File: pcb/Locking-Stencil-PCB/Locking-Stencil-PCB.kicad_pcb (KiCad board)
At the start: 2 copper layers, 64 parts

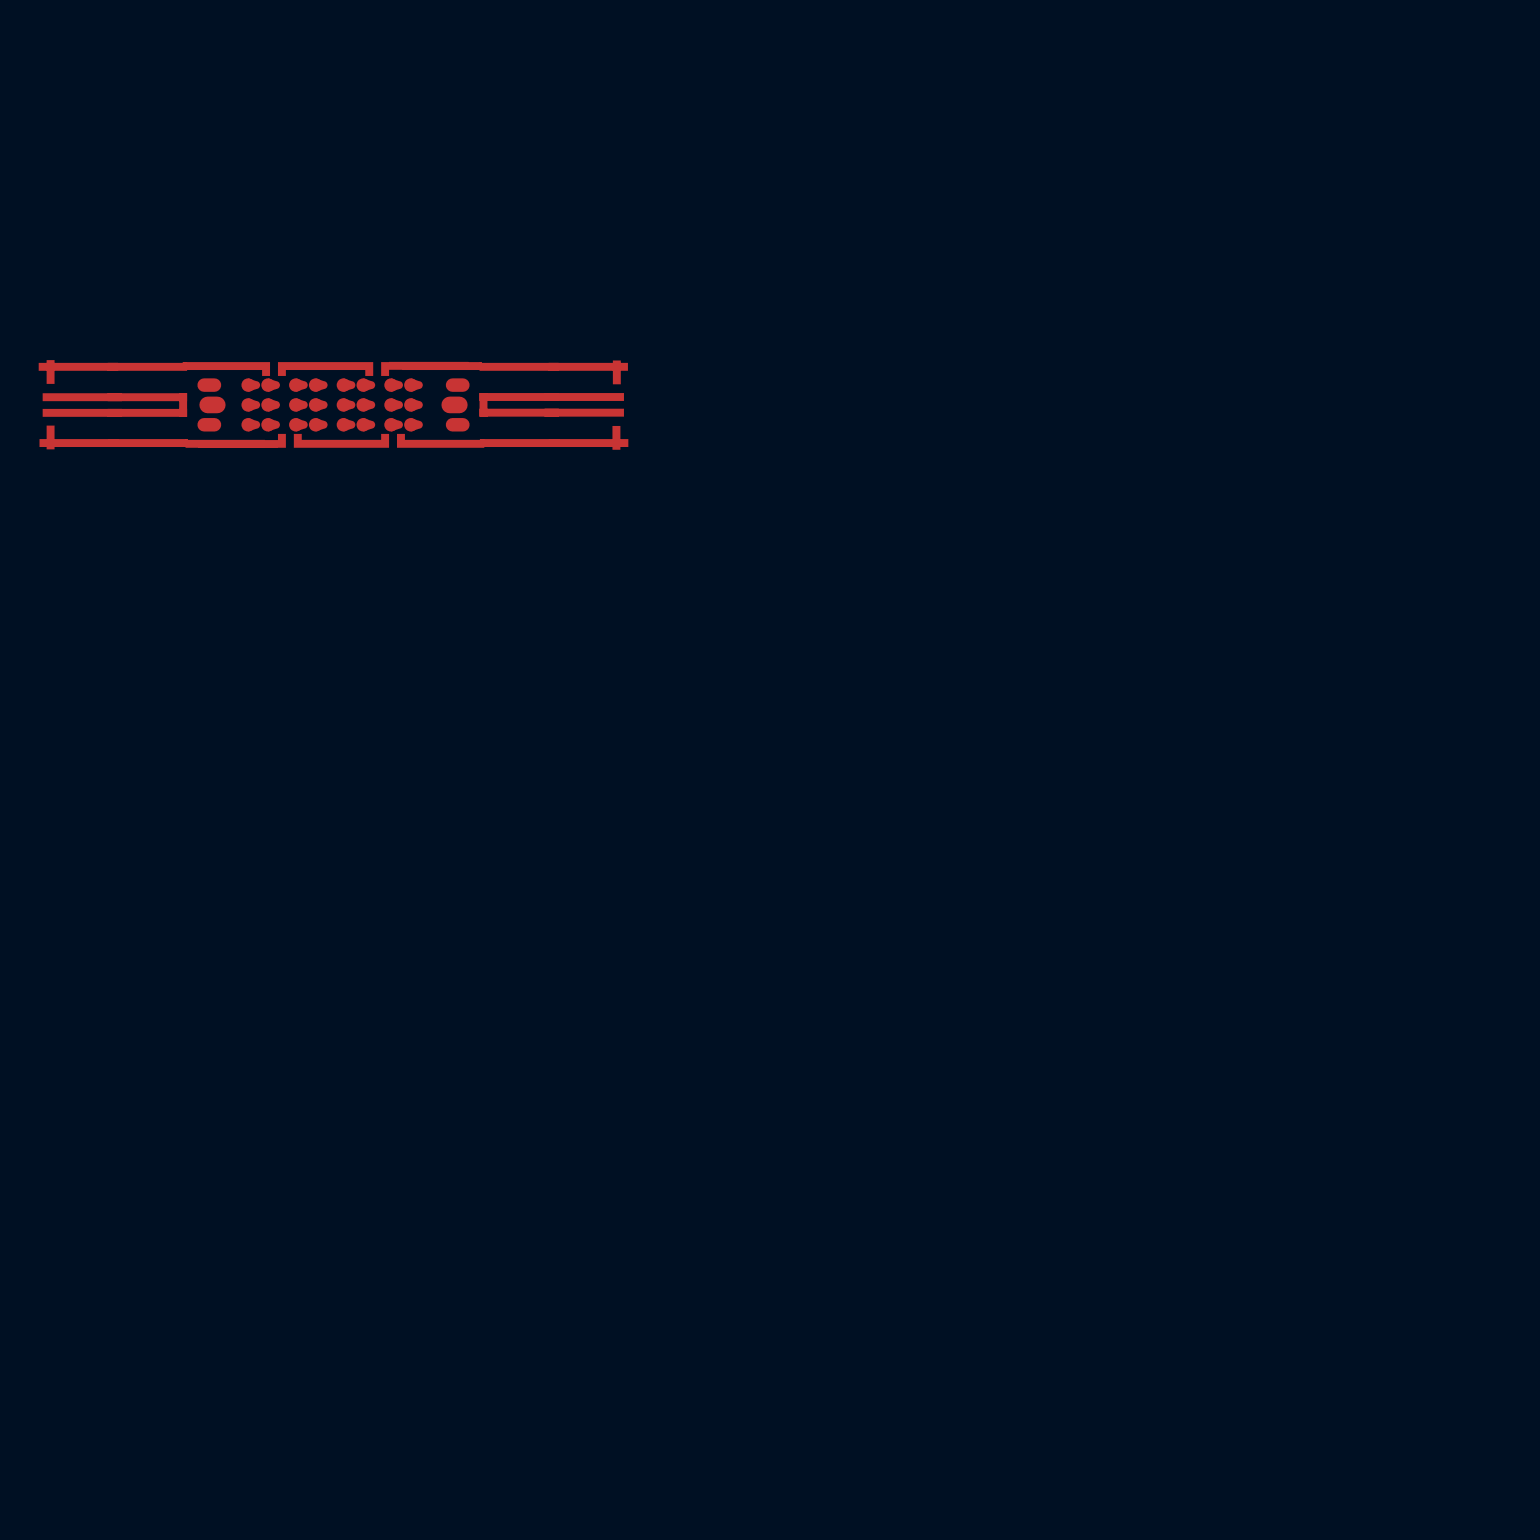
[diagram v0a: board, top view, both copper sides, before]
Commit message: Create stencil order
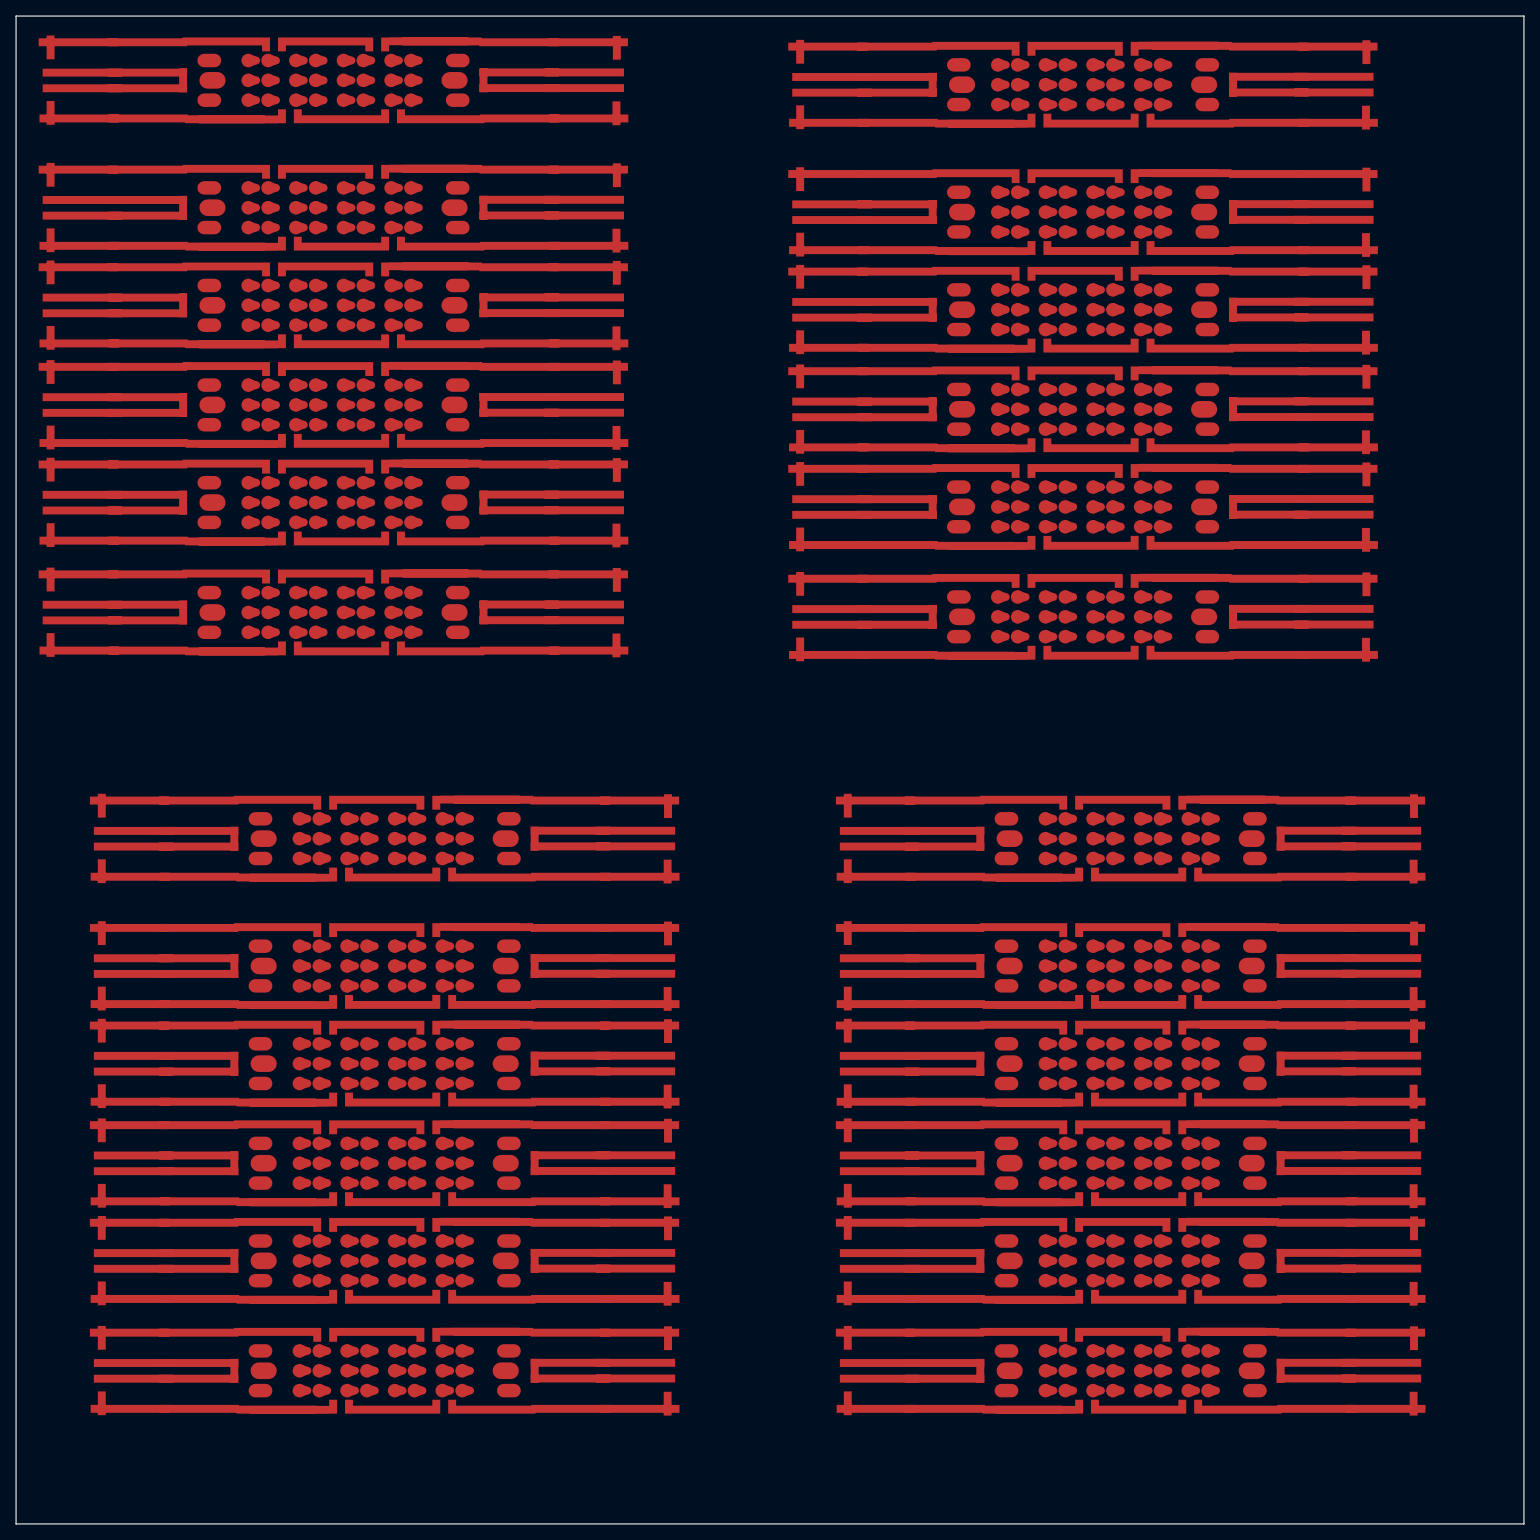
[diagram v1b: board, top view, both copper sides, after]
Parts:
- added REF**: Pad_Cutable_Segment_1mm, 00-stencil-footprint-lib:Pad_Cutable_Segment_1mm, F.Cu at (114.0, 159.1)
- added REF**: Pad_10x1mm, 00-stencil-footprint-lib:Pad_10x1mm, F.Cu at (138.1, 207.3)
- added REF**: Pad_Tapered_d1_1.7mm_d2_1mm_dist_1mm, 00-stencil-footprint-lib:Pad_Tapered_d1_1.7mm_d2_1mm_dist_1mm, F.Cu at (208.2, 195.6)
- added REF**: Pad_10x1mm, 00-stencil-footprint-lib:Pad_10x1mm, F.Cu at (171.0, 71.4)
- added REF**: Pad_Slot_d_1.7mm_dist_1mm, 00-stencil-footprint-lib:Pad_Slot_d_1.7mm_dist_1mm, F.Cu at (216.6, 173.2)
- added REF**: Pad_Slot_d_1.7mm_dist_1mm, 00-stencil-footprint-lib:Pad_Slot_d_1.7mm_dist_1mm, F.Cu at (185.3, 198.1)
- added REF**: Pad_10x1mm, 00-stencil-footprint-lib:Pad_10x1mm, F.Cu at (195.4, 131.1)
- added REF**: Pad_10x1mm, 00-stencil-footprint-lib:Pad_10x1mm, F.Cu at (74.8, 208.3)
- added REF**: Pad_10x1mm, 00-stencil-footprint-lib:Pad_10x1mm, F.Cu at (168.8, 171.2)
- added REF**: Pad_Slot_d_2.1mm_dist_1mm, 00-stencil-footprint-lib:Pad_Slot_d_2.1mm_dist_1mm, F.Cu at (122.2, 170.7)
- added REF**: Pad_10x1mm, 00-stencil-footprint-lib:Pad_10x1mm, F.Cu at (180.8, 131.1)
- added REF**: Pad_Tapered_d1_1.7mm_d2_1mm_dist_1mm, 00-stencil-footprint-lib:Pad_Tapered_d1_1.7mm_d2_1mm_dist_1mm, F.Cu at (110.2, 77.7)
- added REF**: Pad_Slot_d_1.7mm_dist_1mm, 00-stencil-footprint-lib:Pad_Slot_d_1.7mm_dist_1mm, F.Cu at (216.6, 157.2)
- added REF**: Pad_10x1mm, 00-stencil-footprint-lib:Pad_10x1mm, F.Cu at (83.1, 158.9)
- added REF**: Pad_10x1mm, 00-stencil-footprint-lib:Pad_10x1mm, F.Cu at (168.4, 212.2)
- added REF**: Pad_10x1mm, 00-stencil-footprint-lib:Pad_10x1mm, F.Cu at (217.8, 89.5)
- added REF**: Pad_Slot_d_1.7mm_dist_1mm, 00-stencil-footprint-lib:Pad_Slot_d_1.7mm_dist_1mm, F.Cu at (210.6, 62.1)
- added REF**: Pad_3x1mm, 00-stencil-footprint-lib:Pad_3x1mm, F.Cu at (219.8, 170.7)
- added REF**: Pad_10x1mm, 00-stencil-footprint-lib:Pad_10x1mm, F.Cu at (168.8, 194.1)
- added REF**: Pad_Tapered_d1_1.7mm_d2_1mm_dist_1mm, 00-stencil-footprint-lib:Pad_Tapered_d1_1.7mm_d2_1mm_dist_1mm, F.Cu at (196.2, 168.2)
- added REF**: Pad_3x1mm, 00-stencil-footprint-lib:Pad_3x1mm, F.Cu at (175.0, 88.0)
- added REF**: Pad_10x1mm, 00-stencil-footprint-lib:Pad_10x1mm, F.Cu at (107.5, 175.1)
- added REF**: Pad_3x1mm, 00-stencil-footprint-lib:Pad_3x1mm, F.Cu at (219.8, 154.7)
- added REF**: Pad_10x1mm, 00-stencil-footprint-lib:Pad_10x1mm, F.Cu at (171.0, 58.2)
- added REF**: Pad_10x1mm, 00-stencil-footprint-lib:Pad_10x1mm, F.Cu at (92.5, 166.3)
- added REF**: Pad_10x1mm, 00-stencil-footprint-lib:Pad_10x1mm, F.Cu at (162.8, 111.4)
- added REF**: Pad_10x1mm, 00-stencil-footprint-lib:Pad_10x1mm, F.Cu at (131.6, 125.7)
- added REF**: Pad_10x1mm, 00-stencil-footprint-lib:Pad_10x1mm, F.Cu at (214.4, 199.9)
- added REF**: Pad_10x1mm, 00-stencil-footprint-lib:Pad_10x1mm, F.Cu at (223.8, 221.2)
- added REF**: Pad_Tapered_d1_1.7mm_d2_1mm_dist_1mm, 00-stencil-footprint-lib:Pad_Tapered_d1_1.7mm_d2_1mm_dist_1mm, F.Cu at (92.2, 90.0)
- added REF**: Pad_Slot_d_1.7mm_dist_1mm, 00-stencil-footprint-lib:Pad_Slot_d_1.7mm_dist_1mm, F.Cu at (116.2, 114.8)
- added REF**: Pad_Slot_d_1.7mm_dist_1mm, 00-stencil-footprint-lib:Pad_Slot_d_1.7mm_dist_1mm, F.Cu at (116.2, 85.0)
- added REF**: Pad_Tapered_d1_1.7mm_d2_1mm_dist_1mm, 00-stencil-footprint-lib:Pad_Tapered_d1_1.7mm_d2_1mm_dist_1mm, F.Cu at (110.2, 109.8)
- added REF**: Pad_Tapered_d1_1.7mm_d2_1mm_dist_1mm, 00-stencil-footprint-lib:Pad_Tapered_d1_1.7mm_d2_1mm_dist_1mm, F.Cu at (196.2, 62.1)
- added REF**: Pad_Tapered_d1_1.7mm_d2_1mm_dist_1mm, 00-stencil-footprint-lib:Pad_Tapered_d1_1.7mm_d2_1mm_dist_1mm, F.Cu at (204.7, 73.2)
- added REF**: Pad_Tapered_d1_1.7mm_d2_1mm_dist_1mm, 00-stencil-footprint-lib:Pad_Tapered_d1_1.7mm_d2_1mm_dist_1mm, F.Cu at (210.7, 185.5)
- added REF**: Pad_Cutable_Segment_1mm, 00-stencil-footprint-lib:Pad_Cutable_Segment_1mm, F.Cu at (199.9, 96.2)
- added REF**: Pad_10x1mm, 00-stencil-footprint-lib:Pad_10x1mm, F.Cu at (171.0, 86.5)
- added REF**: Pad_10x1mm, 00-stencil-footprint-lib:Pad_10x1mm, F.Cu at (129.9, 175.0)
- added REF**: Pad_10x1mm, 00-stencil-footprint-lib:Pad_10x1mm, F.Cu at (105.5, 150.2)
- added REF**: Pad_10x1mm, 00-stencil-footprint-lib:Pad_10x1mm, F.Cu at (101.0, 130.6)
- added REF**: Pad_10x1mm, 00-stencil-footprint-lib:Pad_10x1mm, F.Cu at (168.4, 175.0)
- added REF**: Pad_10x1mm, 00-stencil-footprint-lib:Pad_10x1mm, F.Cu at (83.0, 191.2)
- added REF**: Pad_Tapered_d1_1.7mm_d2_1mm_dist_1mm, 00-stencil-footprint-lib:Pad_Tapered_d1_1.7mm_d2_1mm_dist_1mm, F.Cu at (198.7, 154.7)
- added REF**: Pad_Tapered_d1_1.7mm_d2_1mm_dist_1mm, 00-stencil-footprint-lib:Pad_Tapered_d1_1.7mm_d2_1mm_dist_1mm, F.Cu at (104.7, 173.2)
- added REF**: Pad_Tapered_d1_1.7mm_d2_1mm_dist_1mm, 00-stencil-footprint-lib:Pad_Tapered_d1_1.7mm_d2_1mm_dist_1mm, F.Cu at (198.7, 90.5)
- added REF**: Pad_Tapered_d1_1.7mm_d2_1mm_dist_1mm, 00-stencil-footprint-lib:Pad_Tapered_d1_1.7mm_d2_1mm_dist_1mm, F.Cu at (96.2, 210.3)
- added REF**: Pad_10x1mm, 00-stencil-footprint-lib:Pad_10x1mm, F.Cu at (120.5, 212.2)
- added REF**: Pad_Tapered_d1_1.7mm_d2_1mm_dist_1mm, 00-stencil-footprint-lib:Pad_Tapered_d1_1.7mm_d2_1mm_dist_1mm, F.Cu at (208.2, 193.1)
- added REF**: Pad_Tapered_d1_1.7mm_d2_1mm_dist_1mm, 00-stencil-footprint-lib:Pad_Tapered_d1_1.7mm_d2_1mm_dist_1mm, F.Cu at (202.2, 75.7)
- added REF**: Pad_Tapered_d1_1.7mm_d2_1mm_dist_1mm, 00-stencil-footprint-lib:Pad_Tapered_d1_1.7mm_d2_1mm_dist_1mm, F.Cu at (108.2, 224.2)
- added REF**: Pad_Tapered_d1_1.7mm_d2_1mm_dist_1mm, 00-stencil-footprint-lib:Pad_Tapered_d1_1.7mm_d2_1mm_dist_1mm, F.Cu at (104.2, 56.6)
- added REF**: Pad_Cutable_Segment_1mm, 00-stencil-footprint-lib:Pad_Cutable_Segment_1mm, F.Cu at (107.5, 130.6)
- added REF**: Pad_10x1mm, 00-stencil-footprint-lib:Pad_10x1mm, F.Cu at (171.0, 125.2)
- added REF**: Pad_10x1mm, 00-stencil-footprint-lib:Pad_10x1mm, F.Cu at (74.8, 169.2)
- added REF**: Pad_10x1mm, 00-stencil-footprint-lib:Pad_10x1mm, F.Cu at (214.2, 166.3)
- added REF**: Pad_Tapered_d1_1.7mm_d2_1mm_dist_1mm, 00-stencil-footprint-lib:Pad_Tapered_d1_1.7mm_d2_1mm_dist_1mm, F.Cu at (108.2, 180.5)
- added REF**: Pad_Cutable_Segment_1mm, 00-stencil-footprint-lib:Pad_Cutable_Segment_1mm, F.Cu at (92.5, 83.0)
- added REF**: Pad_10x1mm, 00-stencil-footprint-lib:Pad_10x1mm, F.Cu at (186.8, 175.1)
- added REF**: Pad_Tapered_d1_1.7mm_d2_1mm_dist_1mm, 00-stencil-footprint-lib:Pad_Tapered_d1_1.7mm_d2_1mm_dist_1mm, F.Cu at (192.7, 100.5)
- added REF**: Pad_10x1mm, 00-stencil-footprint-lib:Pad_10x1mm, F.Cu at (188.4, 212.3)
- added REF**: Pad_10x1mm, 00-stencil-footprint-lib:Pad_10x1mm, F.Cu at (132.2, 79.5)
- added REF**: Pad_Tapered_d1_1.7mm_d2_1mm_dist_1mm, 00-stencil-footprint-lib:Pad_Tapered_d1_1.7mm_d2_1mm_dist_1mm, F.Cu at (198.7, 221.7)
- added REF**: Pad_Slot_d_2.1mm_dist_1mm, 00-stencil-footprint-lib:Pad_Slot_d_2.1mm_dist_1mm, F.Cu at (216.2, 170.7)
- added REF**: Pad_Tapered_d1_1.7mm_d2_1mm_dist_1mm, 00-stencil-footprint-lib:Pad_Tapered_d1_1.7mm_d2_1mm_dist_1mm, F.Cu at (104.7, 207.8)
- added REF**: Pad_10x1mm, 00-stencil-footprint-lib:Pad_10x1mm, F.Cu at (138.6, 203.6)
- added REF**: Pad_Tapered_d1_1.7mm_d2_1mm_dist_1mm, 00-stencil-footprint-lib:Pad_Tapered_d1_1.7mm_d2_1mm_dist_1mm, F.Cu at (98.2, 56.6)
- added REF**: Pad_3x1mm, 00-stencil-footprint-lib:Pad_3x1mm, F.Cu at (136.2, 108.2)
- added REF**: Pad_10x1mm, 00-stencil-footprint-lib:Pad_10x1mm, F.Cu at (162.8, 58.2)
- added REF**: Pad_10x1mm, 00-stencil-footprint-lib:Pad_10x1mm, F.Cu at (214.4, 175.1)
- added REF**: Pad_3x1mm, 00-stencil-footprint-lib:Pad_3x1mm, F.Cu at (70.3, 203.7)
- added REF**: Pad_Tapered_d1_1.7mm_d2_1mm_dist_1mm, 00-stencil-footprint-lib:Pad_Tapered_d1_1.7mm_d2_1mm_dist_1mm, F.Cu at (89.8, 123.7)
- added REF**: Pad_Tapered_d1_1.7mm_d2_1mm_dist_1mm, 00-stencil-footprint-lib:Pad_Tapered_d1_1.7mm_d2_1mm_dist_1mm, F.Cu at (104.7, 210.3)
- added REF**: Pad_3x1mm, 00-stencil-footprint-lib:Pad_3x1mm, F.Cu at (136.2, 79.3)
- added REF**: Pad_Slot_d_1.7mm_dist_1mm, 00-stencil-footprint-lib:Pad_Slot_d_1.7mm_dist_1mm, F.Cu at (216.6, 180.5)
- added REF**: Pad_Tapered_d1_1.7mm_d2_1mm_dist_1mm, 00-stencil-footprint-lib:Pad_Tapered_d1_1.7mm_d2_1mm_dist_1mm, F.Cu at (186.7, 57.1)
- added REF**: Pad_Tapered_d1_1.7mm_d2_1mm_dist_1mm, 00-stencil-footprint-lib:Pad_Tapered_d1_1.7mm_d2_1mm_dist_1mm, F.Cu at (110.2, 126.2)
- added REF**: Pad_10x1mm, 00-stencil-footprint-lib:Pad_10x1mm, F.Cu at (68.0, 63.4)
- added REF**: Pad_Tapered_d1_1.7mm_d2_1mm_dist_1mm, 00-stencil-footprint-lib:Pad_Tapered_d1_1.7mm_d2_1mm_dist_1mm, F.Cu at (102.2, 173.2)
- added REF**: Pad_10x1mm, 00-stencil-footprint-lib:Pad_10x1mm, F.Cu at (123.4, 87.0)
- added REF**: Pad_Slot_d_1.7mm_dist_1mm, 00-stencil-footprint-lib:Pad_Slot_d_1.7mm_dist_1mm, F.Cu at (185.3, 180.5)
- added REF**: Pad_Slot_d_1.7mm_dist_1mm, 00-stencil-footprint-lib:Pad_Slot_d_1.7mm_dist_1mm, F.Cu at (179.3, 78.2)
- added REF**: Pad_Slot_d_2.1mm_dist_1mm, 00-stencil-footprint-lib:Pad_Slot_d_2.1mm_dist_1mm, F.Cu at (122.2, 183.0)
- added REF**: Pad_10x1mm, 00-stencil-footprint-lib:Pad_10x1mm, F.Cu at (232.6, 212.2)
- added REF**: Pad_Tapered_d1_1.7mm_d2_1mm_dist_1mm, 00-stencil-footprint-lib:Pad_Tapered_d1_1.7mm_d2_1mm_dist_1mm, F.Cu at (101.8, 56.6)
- added REF**: Pad_Tapered_d1_1.7mm_d2_1mm_dist_1mm, 00-stencil-footprint-lib:Pad_Tapered_d1_1.7mm_d2_1mm_dist_1mm, F.Cu at (108.2, 173.2)
- added REF**: Pad_3x1mm, 00-stencil-footprint-lib:Pad_3x1mm, F.Cu at (158.3, 104.7)
- added REF**: Pad_Cutable_Segment_1mm, 00-stencil-footprint-lib:Pad_Cutable_Segment_1mm, F.Cu at (112.0, 203.4)
- added REF**: Pad_10x1mm, 00-stencil-footprint-lib:Pad_10x1mm, F.Cu at (232.1, 207.3)
- added REF**: Pad_3x1mm, 00-stencil-footprint-lib:Pad_3x1mm, F.Cu at (125.8, 183.0)
- added REF**: Pad_Tapered_d1_1.7mm_d2_1mm_dist_1mm, 00-stencil-footprint-lib:Pad_Tapered_d1_1.7mm_d2_1mm_dist_1mm, F.Cu at (196.2, 195.6)
- added REF**: Pad_Tapered_d1_1.7mm_d2_1mm_dist_1mm, 00-stencil-footprint-lib:Pad_Tapered_d1_1.7mm_d2_1mm_dist_1mm, F.Cu at (190.2, 73.2)
- added REF**: Pad_Tapered_d1_1.7mm_d2_1mm_dist_1mm, 00-stencil-footprint-lib:Pad_Tapered_d1_1.7mm_d2_1mm_dist_1mm, F.Cu at (96.2, 183.0)
- added REF**: Pad_Slot_d_1.7mm_dist_1mm, 00-stencil-footprint-lib:Pad_Slot_d_1.7mm_dist_1mm, F.Cu at (84.8, 90.0)
- added REF**: Pad_10x1mm, 00-stencil-footprint-lib:Pad_10x1mm, F.Cu at (214.2, 178.6)
- added REF**: Pad_Cutable_Segment_1mm, 00-stencil-footprint-lib:Pad_Cutable_Segment_1mm, F.Cu at (114.0, 175.1)
- added REF**: Pad_Tapered_d1_1.7mm_d2_1mm_dist_1mm, 00-stencil-footprint-lib:Pad_Tapered_d1_1.7mm_d2_1mm_dist_1mm, F.Cu at (190.2, 224.2)
- added REF**: Pad_10x1mm, 00-stencil-footprint-lib:Pad_10x1mm, F.Cu at (138.6, 178.7)
- added REF**: Pad_Tapered_d1_1.7mm_d2_1mm_dist_1mm, 00-stencil-footprint-lib:Pad_Tapered_d1_1.7mm_d2_1mm_dist_1mm, F.Cu at (190.2, 103.0)
- added REF**: Pad_Cutable_Segment_1mm, 00-stencil-footprint-lib:Pad_Cutable_Segment_1mm, F.Cu at (188.9, 105.0)
- added REF**: Pad_Tapered_d1_1.7mm_d2_1mm_dist_1mm, 00-stencil-footprint-lib:Pad_Tapered_d1_1.7mm_d2_1mm_dist_1mm, F.Cu at (98.2, 87.5)
- added REF**: Pad_3x1mm, 00-stencil-footprint-lib:Pad_3x1mm, F.Cu at (158.3, 71.5)
- added REF**: Pad_10x1mm, 00-stencil-footprint-lib:Pad_10x1mm, F.Cu at (232.1, 172.2)
- added REF**: Pad_3x1mm, 00-stencil-footprint-lib:Pad_3x1mm, F.Cu at (164.3, 203.7)
- added REF**: Pad_10x1mm, 00-stencil-footprint-lib:Pad_10x1mm, F.Cu at (120.5, 187.4)
- added REF**: Pad_Tapered_d1_1.7mm_d2_1mm_dist_1mm, 00-stencil-footprint-lib:Pad_Tapered_d1_1.7mm_d2_1mm_dist_1mm, F.Cu at (101.8, 126.2)
- added REF**: Pad_Tapered_d1_1.7mm_d2_1mm_dist_1mm, 00-stencil-footprint-lib:Pad_Tapered_d1_1.7mm_d2_1mm_dist_1mm, F.Cu at (192.7, 85.5)
- added REF**: Pad_10x1mm, 00-stencil-footprint-lib:Pad_10x1mm, F.Cu at (168.8, 206.4)
- added REF**: Pad_3x1mm, 00-stencil-footprint-lib:Pad_3x1mm, F.Cu at (236.6, 212.0)
- added REF**: Pad_Tapered_d1_1.7mm_d2_1mm_dist_1mm, 00-stencil-footprint-lib:Pad_Tapered_d1_1.7mm_d2_1mm_dist_1mm, F.Cu at (96.2, 221.7)
- added REF**: Pad_10x1mm, 00-stencil-footprint-lib:Pad_10x1mm, F.Cu at (223.9, 212.2)
- added REF**: Pad_Tapered_d1_1.7mm_d2_1mm_dist_1mm, 00-stencil-footprint-lib:Pad_Tapered_d1_1.7mm_d2_1mm_dist_1mm, F.Cu at (202.2, 85.5)
- added REF**: Pad_Tapered_d1_1.7mm_d2_1mm_dist_1mm, 00-stencil-footprint-lib:Pad_Tapered_d1_1.7mm_d2_1mm_dist_1mm, F.Cu at (110.7, 152.2)
- added REF**: Pad_Slot_d_2.1mm_dist_1mm, 00-stencil-footprint-lib:Pad_Slot_d_2.1mm_dist_1mm, F.Cu at (85.2, 59.1)
- added REF**: Pad_10x1mm, 00-stencil-footprint-lib:Pad_10x1mm, F.Cu at (83.0, 206.4)
- added REF**: Pad_Slot_d_2.1mm_dist_1mm, 00-stencil-footprint-lib:Pad_Slot_d_2.1mm_dist_1mm, F.Cu at (179.7, 100.5)
- added REF**: Pad_Slot_d_1.7mm_dist_1mm, 00-stencil-footprint-lib:Pad_Slot_d_1.7mm_dist_1mm, F.Cu at (185.3, 210.3)
- added REF**: Pad_10x1mm, 00-stencil-footprint-lib:Pad_10x1mm, F.Cu at (206.4, 71.3)
- added REF**: Pad_10x1mm, 00-stencil-footprint-lib:Pad_10x1mm, F.Cu at (208.2, 55.2)
- added REF**: Pad_Slot_d_1.7mm_dist_1mm, 00-stencil-footprint-lib:Pad_Slot_d_1.7mm_dist_1mm, F.Cu at (91.3, 205.3)
- added REF**: Pad_Tapered_d1_1.7mm_d2_1mm_dist_1mm, 00-stencil-footprint-lib:Pad_Tapered_d1_1.7mm_d2_1mm_dist_1mm, F.Cu at (114.2, 198.1)
- added REF**: Pad_Tapered_d1_1.7mm_d2_1mm_dist_1mm, 00-stencil-footprint-lib:Pad_Tapered_d1_1.7mm_d2_1mm_dist_1mm, F.Cu at (98.7, 207.8)
- added REF**: Pad_10x1mm, 00-stencil-footprint-lib:Pad_10x1mm, F.Cu at (232.1, 209.3)
- added REF**: Pad_Tapered_d1_1.7mm_d2_1mm_dist_1mm, 00-stencil-footprint-lib:Pad_Tapered_d1_1.7mm_d2_1mm_dist_1mm, F.Cu at (186.7, 126.7)
- added REF**: Pad_Tapered_d1_1.7mm_d2_1mm_dist_1mm, 00-stencil-footprint-lib:Pad_Tapered_d1_1.7mm_d2_1mm_dist_1mm, F.Cu at (95.8, 128.7)
- added REF**: Pad_Tapered_d1_1.7mm_d2_1mm_dist_1mm, 00-stencil-footprint-lib:Pad_Tapered_d1_1.7mm_d2_1mm_dist_1mm, F.Cu at (98.2, 112.3)
- added REF**: Pad_Tapered_d1_1.7mm_d2_1mm_dist_1mm, 00-stencil-footprint-lib:Pad_Tapered_d1_1.7mm_d2_1mm_dist_1mm, F.Cu at (116.7, 157.2)
- added REF**: Pad_10x1mm, 00-stencil-footprint-lib:Pad_10x1mm, F.Cu at (232.6, 226.0)
- added REF**: Pad_Tapered_d1_1.7mm_d2_1mm_dist_1mm, 00-stencil-footprint-lib:Pad_Tapered_d1_1.7mm_d2_1mm_dist_1mm, F.Cu at (104.7, 185.5)
- added REF**: Pad_10x1mm, 00-stencil-footprint-lib:Pad_10x1mm, F.Cu at (232.6, 175.0)
- added REF**: Pad_Cutable_Segment_1mm, 00-stencil-footprint-lib:Pad_Cutable_Segment_1mm, F.Cu at (101.0, 212.2)
- added REF**: Pad_Tapered_d1_1.7mm_d2_1mm_dist_1mm, 00-stencil-footprint-lib:Pad_Tapered_d1_1.7mm_d2_1mm_dist_1mm, F.Cu at (98.7, 154.7)
- added REF**: Pad_Tapered_d1_1.7mm_d2_1mm_dist_1mm, 00-stencil-footprint-lib:Pad_Tapered_d1_1.7mm_d2_1mm_dist_1mm, F.Cu at (184.2, 112.8)
- added REF**: Pad_Slot_d_2.1mm_dist_1mm, 00-stencil-footprint-lib:Pad_Slot_d_2.1mm_dist_1mm, F.Cu at (185.7, 207.8)
- added REF**: Pad_Tapered_d1_1.7mm_d2_1mm_dist_1mm, 00-stencil-footprint-lib:Pad_Tapered_d1_1.7mm_d2_1mm_dist_1mm, F.Cu at (101.8, 112.3)
- added REF**: Pad_Tapered_d1_1.7mm_d2_1mm_dist_1mm, 00-stencil-footprint-lib:Pad_Tapered_d1_1.7mm_d2_1mm_dist_1mm, F.Cu at (198.7, 85.5)
- added REF**: Pad_10x1mm, 00-stencil-footprint-lib:Pad_10x1mm, F.Cu at (226.1, 77.2)
- added REF**: Pad_10x1mm, 00-stencil-footprint-lib:Pad_10x1mm, F.Cu at (129.8, 156.1)
- added REF**: Pad_Tapered_d1_1.7mm_d2_1mm_dist_1mm, 00-stencil-footprint-lib:Pad_Tapered_d1_1.7mm_d2_1mm_dist_1mm, F.Cu at (107.8, 114.8)
- added REF**: Pad_10x1mm, 00-stencil-footprint-lib:Pad_10x1mm, F.Cu at (92.5, 191.2)
- added REF**: Pad_Slot_d_1.7mm_dist_1mm, 00-stencil-footprint-lib:Pad_Slot_d_1.7mm_dist_1mm, F.Cu at (116.2, 61.6)
- added REF**: Pad_Cutable_Segment_1mm, 00-stencil-footprint-lib:Pad_Cutable_Segment_1mm, F.Cu at (199.9, 83.6)
- added REF**: Pad_Tapered_d1_1.7mm_d2_1mm_dist_1mm, 00-stencil-footprint-lib:Pad_Tapered_d1_1.7mm_d2_1mm_dist_1mm, F.Cu at (210.7, 224.2)
- added REF**: Pad_Tapered_d1_1.7mm_d2_1mm_dist_1mm, 00-stencil-footprint-lib:Pad_Tapered_d1_1.7mm_d2_1mm_dist_1mm, F.Cu at (108.2, 170.7)
- added REF**: Pad_Tapered_d1_1.7mm_d2_1mm_dist_1mm, 00-stencil-footprint-lib:Pad_Tapered_d1_1.7mm_d2_1mm_dist_1mm, F.Cu at (102.2, 205.3)
- added REF**: Pad_10x1mm, 00-stencil-footprint-lib:Pad_10x1mm, F.Cu at (177.0, 169.2)
- added REF**: Pad_10x1mm, 00-stencil-footprint-lib:Pad_10x1mm, F.Cu at (162.4, 117.2)
- added REF**: Pad_Tapered_d1_1.7mm_d2_1mm_dist_1mm, 00-stencil-footprint-lib:Pad_Tapered_d1_1.7mm_d2_1mm_dist_1mm, F.Cu at (204.7, 62.1)
- added REF**: Pad_10x1mm, 00-stencil-footprint-lib:Pad_10x1mm, F.Cu at (131.6, 88.9)
- added REF**: Pad_10x1mm, 00-stencil-footprint-lib:Pad_10x1mm, F.Cu at (76.5, 126.7)
- added REF**: Pad_3x1mm, 00-stencil-footprint-lib:Pad_3x1mm, F.Cu at (80.5, 112.3)
- added REF**: Pad_10x1mm, 00-stencil-footprint-lib:Pad_10x1mm, F.Cu at (217.9, 92.3)
- added REF**: Pad_Tapered_d1_1.7mm_d2_1mm_dist_1mm, 00-stencil-footprint-lib:Pad_Tapered_d1_1.7mm_d2_1mm_dist_1mm, F.Cu at (196.2, 157.2)
- added REF**: Pad_Slot_d_1.7mm_dist_1mm, 00-stencil-footprint-lib:Pad_Slot_d_1.7mm_dist_1mm, F.Cu at (84.8, 85.0)
- added REF**: Pad_10x1mm, 00-stencil-footprint-lib:Pad_10x1mm, F.Cu at (138.1, 195.1)
- added REF**: Pad_Tapered_d1_1.7mm_d2_1mm_dist_1mm, 00-stencil-footprint-lib:Pad_Tapered_d1_1.7mm_d2_1mm_dist_1mm, F.Cu at (98.2, 77.7)
- added REF**: Pad_Slot_d_2.1mm_dist_1mm, 00-stencil-footprint-lib:Pad_Slot_d_2.1mm_dist_1mm, F.Cu at (210.2, 126.7)
- added REF**: Pad_Tapered_d1_1.7mm_d2_1mm_dist_1mm, 00-stencil-footprint-lib:Pad_Tapered_d1_1.7mm_d2_1mm_dist_1mm, F.Cu at (104.2, 128.7)
- added REF**: Pad_10x1mm, 00-stencil-footprint-lib:Pad_10x1mm, F.Cu at (118.5, 217.3)
- added REF**: Pad_Slot_d_1.7mm_dist_1mm, 00-stencil-footprint-lib:Pad_Slot_d_1.7mm_dist_1mm, F.Cu at (122.6, 198.1)
- added REF**: Pad_Cutable_Segment_1mm, 00-stencil-footprint-lib:Pad_Cutable_Segment_1mm, F.Cu at (92.5, 121.8)
- added REF**: Pad_Slot_d_1.7mm_dist_1mm, 00-stencil-footprint-lib:Pad_Slot_d_1.7mm_dist_1mm, F.Cu at (216.6, 219.2)
- added REF**: Pad_10x1mm, 00-stencil-footprint-lib:Pad_10x1mm, F.Cu at (131.6, 58.6)
- added REF**: Pad_10x1mm, 00-stencil-footprint-lib:Pad_10x1mm, F.Cu at (195.4, 92.4)
- added REF**: Pad_Tapered_d1_1.7mm_d2_1mm_dist_1mm, 00-stencil-footprint-lib:Pad_Tapered_d1_1.7mm_d2_1mm_dist_1mm, F.Cu at (98.2, 61.6)
- added REF**: Pad_10x1mm, 00-stencil-footprint-lib:Pad_10x1mm, F.Cu at (74.3, 178.7)
- added REF**: Pad_Tapered_d1_1.7mm_d2_1mm_dist_1mm, 00-stencil-footprint-lib:Pad_Tapered_d1_1.7mm_d2_1mm_dist_1mm, F.Cu at (192.7, 157.2)
- added REF**: Pad_Tapered_d1_1.7mm_d2_1mm_dist_1mm, 00-stencil-footprint-lib:Pad_Tapered_d1_1.7mm_d2_1mm_dist_1mm, F.Cu at (198.7, 73.2)
- added REF**: Pad_10x1mm, 00-stencil-footprint-lib:Pad_10x1mm, F.Cu at (199.4, 217.3)
- added REF**: Pad_10x1mm, 00-stencil-footprint-lib:Pad_10x1mm, F.Cu at (129.9, 212.2)
- added REF**: Pad_Slot_d_1.7mm_dist_1mm, 00-stencil-footprint-lib:Pad_Slot_d_1.7mm_dist_1mm, F.Cu at (185.3, 205.3)
- added REF**: Pad_10x1mm, 00-stencil-footprint-lib:Pad_10x1mm, F.Cu at (177.1, 212.2)
- added REF**: Pad_3x1mm, 00-stencil-footprint-lib:Pad_3x1mm, F.Cu at (119.4, 87.5)
- added REF**: Pad_Tapered_d1_1.7mm_d2_1mm_dist_1mm, 00-stencil-footprint-lib:Pad_Tapered_d1_1.7mm_d2_1mm_dist_1mm, F.Cu at (186.7, 59.6)
- added REF**: Pad_Tapered_d1_1.7mm_d2_1mm_dist_1mm, 00-stencil-footprint-lib:Pad_Tapered_d1_1.7mm_d2_1mm_dist_1mm, F.Cu at (98.7, 221.7)
- added REF**: Pad_Tapered_d1_1.7mm_d2_1mm_dist_1mm, 00-stencil-footprint-lib:Pad_Tapered_d1_1.7mm_d2_1mm_dist_1mm, F.Cu at (89.8, 112.3)
- added REF**: Pad_10x1mm, 00-stencil-footprint-lib:Pad_10x1mm, F.Cu at (226.6, 96.2)
- added REF**: Pad_Tapered_d1_1.7mm_d2_1mm_dist_1mm, 00-stencil-footprint-lib:Pad_Tapered_d1_1.7mm_d2_1mm_dist_1mm, F.Cu at (196.2, 221.7)
- added REF**: Pad_Cutable_Segment_1mm, 00-stencil-footprint-lib:Pad_Cutable_Segment_1mm, F.Cu at (114.0, 187.4)
- added REF**: Pad_Cutable_Segment_1mm, 00-stencil-footprint-lib:Pad_Cutable_Segment_1mm, F.Cu at (99.0, 166.3)
- added REF**: Pad_10x1mm, 00-stencil-footprint-lib:Pad_10x1mm, F.Cu at (223.8, 195.1)
- added REF**: Pad_Tapered_d1_1.7mm_d2_1mm_dist_1mm, 00-stencil-footprint-lib:Pad_Tapered_d1_1.7mm_d2_1mm_dist_1mm, F.Cu at (208.2, 185.5)
- added REF**: Pad_10x1mm, 00-stencil-footprint-lib:Pad_10x1mm, F.Cu at (188.4, 159.1)
- added REF**: Pad_10x1mm, 00-stencil-footprint-lib:Pad_10x1mm, F.Cu at (223.8, 150.3)
- added REF**: Pad_Tapered_d1_1.7mm_d2_1mm_dist_1mm, 00-stencil-footprint-lib:Pad_Tapered_d1_1.7mm_d2_1mm_dist_1mm, F.Cu at (95.8, 112.3)
- added REF**: Pad_Tapered_d1_1.7mm_d2_1mm_dist_1mm, 00-stencil-footprint-lib:Pad_Tapered_d1_1.7mm_d2_1mm_dist_1mm, F.Cu at (92.2, 112.3)
- added REF**: Pad_Tapered_d1_1.7mm_d2_1mm_dist_1mm, 00-stencil-footprint-lib:Pad_Tapered_d1_1.7mm_d2_1mm_dist_1mm, F.Cu at (190.2, 78.2)
- added REF**: Pad_Tapered_d1_1.7mm_d2_1mm_dist_1mm, 00-stencil-footprint-lib:Pad_Tapered_d1_1.7mm_d2_1mm_dist_1mm, F.Cu at (114.2, 168.2)
- added REF**: Pad_10x1mm, 00-stencil-footprint-lib:Pad_10x1mm, F.Cu at (162.8, 88.5)
- added REF**: Pad_3x1mm, 00-stencil-footprint-lib:Pad_3x1mm, F.Cu at (158.3, 122.5)
- added REF**: Pad_10x1mm, 00-stencil-footprint-lib:Pad_10x1mm, F.Cu at (212.4, 217.3)
- added REF**: Pad_Slot_d_1.7mm_dist_1mm, 00-stencil-footprint-lib:Pad_Slot_d_1.7mm_dist_1mm, F.Cu at (185.3, 168.2)
- added REF**: Pad_3x1mm, 00-stencil-footprint-lib:Pad_3x1mm, F.Cu at (213.8, 59.6)
- added REF**: Pad_Tapered_d1_1.7mm_d2_1mm_dist_1mm, 00-stencil-footprint-lib:Pad_Tapered_d1_1.7mm_d2_1mm_dist_1mm, F.Cu at (192.7, 98.0)
- added REF**: Pad_Tapered_d1_1.7mm_d2_1mm_dist_1mm, 00-stencil-footprint-lib:Pad_Tapered_d1_1.7mm_d2_1mm_dist_1mm, F.Cu at (116.7, 207.8)
- added REF**: Pad_10x1mm, 00-stencil-footprint-lib:Pad_10x1mm, F.Cu at (138.6, 199.8)
- added REF**: Pad_10x1mm, 00-stencil-footprint-lib:Pad_10x1mm, F.Cu at (131.6, 111.8)
- added REF**: Pad_3x1mm, 00-stencil-footprint-lib:Pad_3x1mm, F.Cu at (119.4, 59.1)
- added REF**: Pad_10x1mm, 00-stencil-footprint-lib:Pad_10x1mm, F.Cu at (83.0, 181.5)
- added REF**: Pad_10x1mm, 00-stencil-footprint-lib:Pad_10x1mm, F.Cu at (195.4, 117.2)
- added REF**: Pad_Slot_d_1.7mm_dist_1mm, 00-stencil-footprint-lib:Pad_Slot_d_1.7mm_dist_1mm, F.Cu at (185.3, 185.5)
- added REF**: Pad_10x1mm, 00-stencil-footprint-lib:Pad_10x1mm, F.Cu at (83.0, 150.3)
- added REF**: Pad_10x1mm, 00-stencil-footprint-lib:Pad_10x1mm, F.Cu at (177.0, 153.2)
- added REF**: Pad_Tapered_d1_1.7mm_d2_1mm_dist_1mm, 00-stencil-footprint-lib:Pad_Tapered_d1_1.7mm_d2_1mm_dist_1mm, F.Cu at (202.2, 193.1)
- added REF**: Pad_Tapered_d1_1.7mm_d2_1mm_dist_1mm, 00-stencil-footprint-lib:Pad_Tapered_d1_1.7mm_d2_1mm_dist_1mm, F.Cu at (107.8, 87.5)
- added REF**: Pad_Slot_d_1.7mm_dist_1mm, 00-stencil-footprint-lib:Pad_Slot_d_1.7mm_dist_1mm, F.Cu at (122.6, 168.2)
- added REF**: Pad_Tapered_d1_1.7mm_d2_1mm_dist_1mm, 00-stencil-footprint-lib:Pad_Tapered_d1_1.7mm_d2_1mm_dist_1mm, F.Cu at (104.2, 123.7)
- added REF**: Pad_10x1mm, 00-stencil-footprint-lib:Pad_10x1mm, F.Cu at (86.3, 63.5)
- added REF**: Pad_Tapered_d1_1.7mm_d2_1mm_dist_1mm, 00-stencil-footprint-lib:Pad_Tapered_d1_1.7mm_d2_1mm_dist_1mm, F.Cu at (202.2, 100.5)
- added REF**: Pad_Tapered_d1_1.7mm_d2_1mm_dist_1mm, 00-stencil-footprint-lib:Pad_Tapered_d1_1.7mm_d2_1mm_dist_1mm, F.Cu at (107.8, 126.2)
- added REF**: Pad_10x1mm, 00-stencil-footprint-lib:Pad_10x1mm, F.Cu at (171.0, 101.0)
- added REF**: Pad_Tapered_d1_1.7mm_d2_1mm_dist_1mm, 00-stencil-footprint-lib:Pad_Tapered_d1_1.7mm_d2_1mm_dist_1mm, F.Cu at (190.2, 115.3)
- added REF**: Pad_Tapered_d1_1.7mm_d2_1mm_dist_1mm, 00-stencil-footprint-lib:Pad_Tapered_d1_1.7mm_d2_1mm_dist_1mm, F.Cu at (92.2, 59.1)
- added REF**: Pad_3x1mm, 00-stencil-footprint-lib:Pad_3x1mm, F.Cu at (125.8, 221.7)
- added REF**: Pad_10x1mm, 00-stencil-footprint-lib:Pad_10x1mm, F.Cu at (74.8, 181.5)
- added REF**: Pad_Tapered_d1_1.7mm_d2_1mm_dist_1mm, 00-stencil-footprint-lib:Pad_Tapered_d1_1.7mm_d2_1mm_dist_1mm, F.Cu at (184.2, 85.5)
- added REF**: Pad_10x1mm, 00-stencil-footprint-lib:Pad_10x1mm, F.Cu at (123.5, 63.4)
- added REF**: Pad_3x1mm, 00-stencil-footprint-lib:Pad_3x1mm, F.Cu at (236.6, 187.2)
- added REF**: Pad_Slot_d_1.7mm_dist_1mm, 00-stencil-footprint-lib:Pad_Slot_d_1.7mm_dist_1mm, F.Cu at (84.8, 128.7)
- added REF**: Pad_Cutable_Segment_1mm, 00-stencil-footprint-lib:Pad_Cutable_Segment_1mm, F.Cu at (186.9, 108.5)
- added REF**: Pad_3x1mm, 00-stencil-footprint-lib:Pad_3x1mm, F.Cu at (213.8, 100.5)
- added REF**: Pad_10x1mm, 00-stencil-footprint-lib:Pad_10x1mm, F.Cu at (74.4, 199.8)
- added REF**: Pad_10x1mm, 00-stencil-footprint-lib:Pad_10x1mm, F.Cu at (199.4, 166.3)
- added REF**: Pad_10x1mm, 00-stencil-footprint-lib:Pad_10x1mm, F.Cu at (177.1, 158.9)
- added REF**: Pad_3x1mm, 00-stencil-footprint-lib:Pad_3x1mm, F.Cu at (63.9, 116.4)
- added REF**: Pad_Tapered_d1_1.7mm_d2_1mm_dist_1mm, 00-stencil-footprint-lib:Pad_Tapered_d1_1.7mm_d2_1mm_dist_1mm, F.Cu at (190.2, 185.5)
- added REF**: Pad_10x1mm, 00-stencil-footprint-lib:Pad_10x1mm, F.Cu at (131.6, 127.6)
- added REF**: Pad_Tapered_d1_1.7mm_d2_1mm_dist_1mm, 00-stencil-footprint-lib:Pad_Tapered_d1_1.7mm_d2_1mm_dist_1mm, F.Cu at (198.7, 112.8)
- added REF**: Pad_10x1mm, 00-stencil-footprint-lib:Pad_10x1mm, F.Cu at (217.8, 102.0)
- added REF**: Pad_Cutable_Segment_1mm, 00-stencil-footprint-lib:Pad_Cutable_Segment_1mm, F.Cu at (205.9, 166.3)
- added REF**: Pad_10x1mm, 00-stencil-footprint-lib:Pad_10x1mm, F.Cu at (232.1, 221.2)
- added REF**: Pad_Tapered_d1_1.7mm_d2_1mm_dist_1mm, 00-stencil-footprint-lib:Pad_Tapered_d1_1.7mm_d2_1mm_dist_1mm, F.Cu at (196.2, 126.7)
- added REF**: Pad_Tapered_d1_1.7mm_d2_1mm_dist_1mm, 00-stencil-footprint-lib:Pad_Tapered_d1_1.7mm_d2_1mm_dist_1mm, F.Cu at (202.2, 168.2)
- added REF**: Pad_Tapered_d1_1.7mm_d2_1mm_dist_1mm, 00-stencil-footprint-lib:Pad_Tapered_d1_1.7mm_d2_1mm_dist_1mm, F.Cu at (101.8, 61.6)
- added REF**: Pad_Tapered_d1_1.7mm_d2_1mm_dist_1mm, 00-stencil-footprint-lib:Pad_Tapered_d1_1.7mm_d2_1mm_dist_1mm, F.Cu at (89.8, 90.0)
- added REF**: Pad_Tapered_d1_1.7mm_d2_1mm_dist_1mm, 00-stencil-footprint-lib:Pad_Tapered_d1_1.7mm_d2_1mm_dist_1mm, F.Cu at (202.2, 183.0)
- added REF**: Pad_Tapered_d1_1.7mm_d2_1mm_dist_1mm, 00-stencil-footprint-lib:Pad_Tapered_d1_1.7mm_d2_1mm_dist_1mm, F.Cu at (108.2, 183.0)
- added REF**: Pad_3x1mm, 00-stencil-footprint-lib:Pad_3x1mm, F.Cu at (136.2, 116.5)
- added REF**: Pad_Slot_d_1.7mm_dist_1mm, 00-stencil-footprint-lib:Pad_Slot_d_1.7mm_dist_1mm, F.Cu at (91.3, 173.2)
- added REF**: Pad_3x1mm, 00-stencil-footprint-lib:Pad_3x1mm, F.Cu at (181.0, 183.0)
- added REF**: Pad_Tapered_d1_1.7mm_d2_1mm_dist_1mm, 00-stencil-footprint-lib:Pad_Tapered_d1_1.7mm_d2_1mm_dist_1mm, F.Cu at (102.2, 221.7)
- added REF**: Pad_Tapered_d1_1.7mm_d2_1mm_dist_1mm, 00-stencil-footprint-lib:Pad_Tapered_d1_1.7mm_d2_1mm_dist_1mm, F.Cu at (184.2, 88.0)
- added REF**: Pad_Tapered_d1_1.7mm_d2_1mm_dist_1mm, 00-stencil-footprint-lib:Pad_Tapered_d1_1.7mm_d2_1mm_dist_1mm, F.Cu at (198.7, 173.2)
- added REF**: Pad_Slot_d_1.7mm_dist_1mm, 00-stencil-footprint-lib:Pad_Slot_d_1.7mm_dist_1mm, F.Cu at (210.6, 103.0)
- added REF**: Pad_Tapered_d1_1.7mm_d2_1mm_dist_1mm, 00-stencil-footprint-lib:Pad_Tapered_d1_1.7mm_d2_1mm_dist_1mm, F.Cu at (104.2, 77.7)
- added REF**: Pad_10x1mm, 00-stencil-footprint-lib:Pad_10x1mm, F.Cu at (177.0, 150.3)
- added REF**: Pad_Tapered_d1_1.7mm_d2_1mm_dist_1mm, 00-stencil-footprint-lib:Pad_Tapered_d1_1.7mm_d2_1mm_dist_1mm, F.Cu at (202.2, 103.0)
- added REF**: Pad_10x1mm, 00-stencil-footprint-lib:Pad_10x1mm, F.Cu at (74.8, 206.4)
- added REF**: Pad_Tapered_d1_1.7mm_d2_1mm_dist_1mm, 00-stencil-footprint-lib:Pad_Tapered_d1_1.7mm_d2_1mm_dist_1mm, F.Cu at (101.8, 72.7)
- added REF**: Pad_Tapered_d1_1.7mm_d2_1mm_dist_1mm, 00-stencil-footprint-lib:Pad_Tapered_d1_1.7mm_d2_1mm_dist_1mm, F.Cu at (192.7, 168.2)
- added REF**: Pad_Tapered_d1_1.7mm_d2_1mm_dist_1mm, 00-stencil-footprint-lib:Pad_Tapered_d1_1.7mm_d2_1mm_dist_1mm, F.Cu at (196.2, 88.0)
- added REF**: Pad_3x1mm, 00-stencil-footprint-lib:Pad_3x1mm, F.Cu at (136.2, 63.2)
- added REF**: Pad_3x1mm, 00-stencil-footprint-lib:Pad_3x1mm, F.Cu at (175.0, 59.6)
- added REF**: Pad_Tapered_d1_1.7mm_d2_1mm_dist_1mm, 00-stencil-footprint-lib:Pad_Tapered_d1_1.7mm_d2_1mm_dist_1mm, F.Cu at (190.2, 210.3)
- added REF**: Pad_Tapered_d1_1.7mm_d2_1mm_dist_1mm, 00-stencil-footprint-lib:Pad_Tapered_d1_1.7mm_d2_1mm_dist_1mm, F.Cu at (196.2, 129.2)
- added REF**: Pad_10x1mm, 00-stencil-footprint-lib:Pad_10x1mm, F.Cu at (226.6, 83.7)
- added REF**: Pad_Tapered_d1_1.7mm_d2_1mm_dist_1mm, 00-stencil-footprint-lib:Pad_Tapered_d1_1.7mm_d2_1mm_dist_1mm, F.Cu at (110.7, 195.6)
- added REF**: Pad_Slot_d_1.7mm_dist_1mm, 00-stencil-footprint-lib:Pad_Slot_d_1.7mm_dist_1mm, F.Cu at (179.3, 110.3)
- added REF**: Pad_Tapered_d1_1.7mm_d2_1mm_dist_1mm, 00-stencil-footprint-lib:Pad_Tapered_d1_1.7mm_d2_1mm_dist_1mm, F.Cu at (107.8, 85.0)
- added REF**: Pad_10x1mm, 00-stencil-footprint-lib:Pad_10x1mm, F.Cu at (99.0, 70.8)
- added REF**: Pad_10x1mm, 00-stencil-footprint-lib:Pad_10x1mm, F.Cu at (83.0, 203.6)
- added REF**: Pad_3x1mm, 00-stencil-footprint-lib:Pad_3x1mm, F.Cu at (175.0, 100.5)
- added REF**: Pad_10x1mm, 00-stencil-footprint-lib:Pad_10x1mm, F.Cu at (74.4, 158.9)
- added REF**: Pad_Slot_d_1.7mm_dist_1mm, 00-stencil-footprint-lib:Pad_Slot_d_1.7mm_dist_1mm, F.Cu at (179.3, 57.1)
- added REF**: Pad_10x1mm, 00-stencil-footprint-lib:Pad_10x1mm, F.Cu at (193.4, 108.5)
- added REF**: Pad_Tapered_d1_1.7mm_d2_1mm_dist_1mm, 00-stencil-footprint-lib:Pad_Tapered_d1_1.7mm_d2_1mm_dist_1mm, F.Cu at (116.7, 185.5)
- added REF**: Pad_3x1mm, 00-stencil-footprint-lib:Pad_3x1mm, F.Cu at (230.6, 104.7)
- added REF**: Pad_Tapered_d1_1.7mm_d2_1mm_dist_1mm, 00-stencil-footprint-lib:Pad_Tapered_d1_1.7mm_d2_1mm_dist_1mm, F.Cu at (104.2, 112.3)
- added REF**: Pad_10x1mm, 00-stencil-footprint-lib:Pad_10x1mm, F.Cu at (138.6, 150.3)
- added REF**: Pad_3x1mm, 00-stencil-footprint-lib:Pad_3x1mm, F.Cu at (63.9, 130.2)
- added REF**: Pad_10x1mm, 00-stencil-footprint-lib:Pad_10x1mm, F.Cu at (177.0, 194.1)
- added REF**: Pad_10x1mm, 00-stencil-footprint-lib:Pad_10x1mm, F.Cu at (76.7, 130.4)
- added REF**: Pad_10x1mm, 00-stencil-footprint-lib:Pad_10x1mm, F.Cu at (123.4, 111.8)
- added REF**: Pad_Tapered_d1_1.7mm_d2_1mm_dist_1mm, 00-stencil-footprint-lib:Pad_Tapered_d1_1.7mm_d2_1mm_dist_1mm, F.Cu at (108.2, 154.7)
- added REF**: Pad_Tapered_d1_1.7mm_d2_1mm_dist_1mm, 00-stencil-footprint-lib:Pad_Tapered_d1_1.7mm_d2_1mm_dist_1mm, F.Cu at (204.7, 157.2)
- added REF**: Pad_Tapered_d1_1.7mm_d2_1mm_dist_1mm, 00-stencil-footprint-lib:Pad_Tapered_d1_1.7mm_d2_1mm_dist_1mm, F.Cu at (198.7, 88.0)
- added REF**: Pad_Slot_d_2.1mm_dist_1mm, 00-stencil-footprint-lib:Pad_Slot_d_2.1mm_dist_1mm, F.Cu at (179.7, 75.7)
- added REF**: Pad_Cutable_Segment_1mm, 00-stencil-footprint-lib:Pad_Cutable_Segment_1mm, F.Cu at (105.5, 121.8)
- added REF**: Pad_3x1mm, 00-stencil-footprint-lib:Pad_3x1mm, F.Cu at (236.6, 225.8)
- added REF**: Pad_10x1mm, 00-stencil-footprint-lib:Pad_10x1mm, F.Cu at (114.0, 130.6)
- added REF**: Pad_Cutable_Segment_1mm, 00-stencil-footprint-lib:Pad_Cutable_Segment_1mm, F.Cu at (205.9, 150.2)
- added REF**: Pad_Tapered_d1_1.7mm_d2_1mm_dist_1mm, 00-stencil-footprint-lib:Pad_Tapered_d1_1.7mm_d2_1mm_dist_1mm, F.Cu at (116.7, 154.7)
- added REF**: Pad_3x1mm, 00-stencil-footprint-lib:Pad_3x1mm, F.Cu at (158.3, 117.0)
- added REF**: Pad_10x1mm, 00-stencil-footprint-lib:Pad_10x1mm, F.Cu at (99.0, 54.7)
- added REF**: Pad_10x1mm, 00-stencil-footprint-lib:Pad_10x1mm, F.Cu at (180.8, 92.4)
- added REF**: Pad_Tapered_d1_1.7mm_d2_1mm_dist_1mm, 00-stencil-footprint-lib:Pad_Tapered_d1_1.7mm_d2_1mm_dist_1mm, F.Cu at (208.2, 224.2)
- added REF**: Pad_10x1mm, 00-stencil-footprint-lib:Pad_10x1mm, F.Cu at (123.4, 54.8)
- added REF**: Pad_Tapered_d1_1.7mm_d2_1mm_dist_1mm, 00-stencil-footprint-lib:Pad_Tapered_d1_1.7mm_d2_1mm_dist_1mm, F.Cu at (196.2, 183.0)
- added REF**: Pad_Tapered_d1_1.7mm_d2_1mm_dist_1mm, 00-stencil-footprint-lib:Pad_Tapered_d1_1.7mm_d2_1mm_dist_1mm, F.Cu at (95.8, 109.8)
- added REF**: Pad_Tapered_d1_1.7mm_d2_1mm_dist_1mm, 00-stencil-footprint-lib:Pad_Tapered_d1_1.7mm_d2_1mm_dist_1mm, F.Cu at (96.2, 170.7)
- added REF**: Pad_Tapered_d1_1.7mm_d2_1mm_dist_1mm, 00-stencil-footprint-lib:Pad_Tapered_d1_1.7mm_d2_1mm_dist_1mm, F.Cu at (190.2, 129.2)
- added REF**: Pad_Tapered_d1_1.7mm_d2_1mm_dist_1mm, 00-stencil-footprint-lib:Pad_Tapered_d1_1.7mm_d2_1mm_dist_1mm, F.Cu at (101.8, 123.7)
- added REF**: Pad_10x1mm, 00-stencil-footprint-lib:Pad_10x1mm, F.Cu at (206.4, 55.2)
- added REF**: Pad_10x1mm, 00-stencil-footprint-lib:Pad_10x1mm, F.Cu at (120.5, 159.1)
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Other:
- board outline added: 190 x 190 mm
